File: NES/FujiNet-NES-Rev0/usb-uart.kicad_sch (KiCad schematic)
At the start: 13 parts, among them J3 USB-C, U10 CP2102N-A02-GQFN28, U11 UMH3N

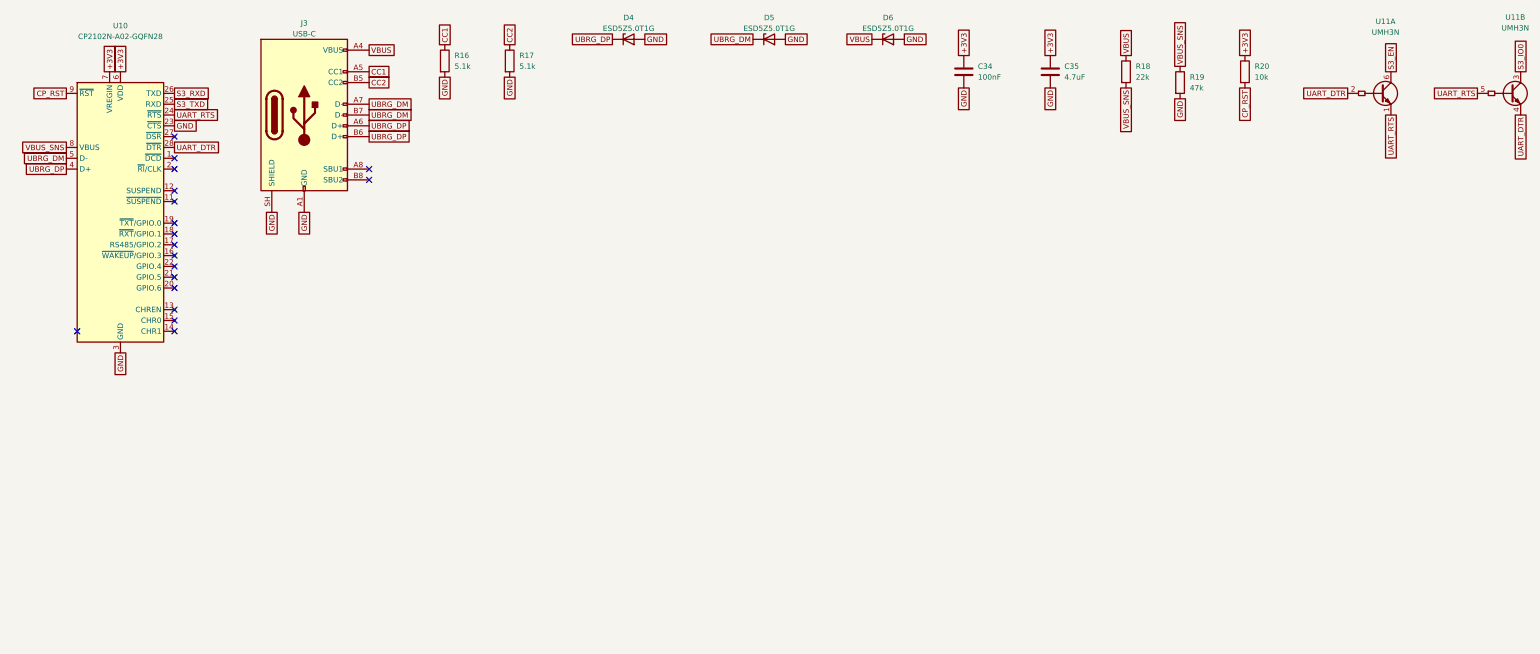
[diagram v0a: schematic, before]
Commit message: Nes rev0 (#48)
* NES: add the FujiNet-NES-Rev0 schematic

RP2354B on the 5 V cart bus with two AS6C4008-55 SRAMs (PRG, CHR) whose
bank lines come from the RP's PIO, 74HCT595/253/14/00/32 glue, and the
Astrocade Rev0 ESP32-S3, USB-UART and power sheets carried over.
Generated from tools/design.py the same way as Astrocade/rev0; ERC
reports no violations and tools/check_nets.py checks every GPIO, SRAM
line and decode equation against fujinet-firmware's nes_cart.h and
fujiversal-nes.h.

Schematic only: no layout, no board built, nothing run on a console.
The edge pinout follows the nesdev Cartridge connector page (pin 37 is
SYSTEM CLK, 2.50 mm pitch).

Co-Authored-By: Claude Fable 5.1 <noreply@anthropic.com>

* NES Rev0: audit the schematic with kicad-happy and redo it

Datasheet-backed review of the first Rev0 schematic (kicad-happy analyzer,
ngspice, 28 deep-review findings all evidence-gated, 453 netlist checks
against fujinet-firmware nes-bringup) and the fixes it called for:

- edge footprint was mirrored (pin 1 west); nesdev and two measured
  NES-EWROM-01 references put pin 1 east on the label side. Fingers are now
  2.0 x 12 mm (ends 3.0 at +/-44.25), 2.50 pitch, copper 1.0-13.0 mm in,
  Nintendo's front/back mask depths
- RP2350 pads are 5 V-tolerant only while IOVDD is powered: the IOVDD group
  moves to an AP2112K (20 us) rail +3V3_RP; VREG_VIN stays on the buck
- 74HCT595 /OE = NAND(PWR_OK, POR) with 100k pull-downs on every bit, so
  the register cannot enable the SRAMs before the RP loads it or while
  the console is off
- PRG /WE = NAND4(M2, ROMSEL, !R/W, PRG_WE_EN) on a CD74HCT20, one gate
  after M2 (was three after the console's /ROMSEL decoder vs ~30 ns hold)
- CIRAM /CE through the 74HCT253's second half, tri-stated by PWR_OK_N
- console 5 V through an AO3401A P-FET (gate = VBUS) instead of a Schottky
- console-sense divider 22k/100k (TI 74HCT14 VT+ reaches 0.70 x VCC)
- WS2812B-2020 on +5V (datasheet VDD 3.7-5.3 V, VIH 2.7 V)
- VBUS decoupling at t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
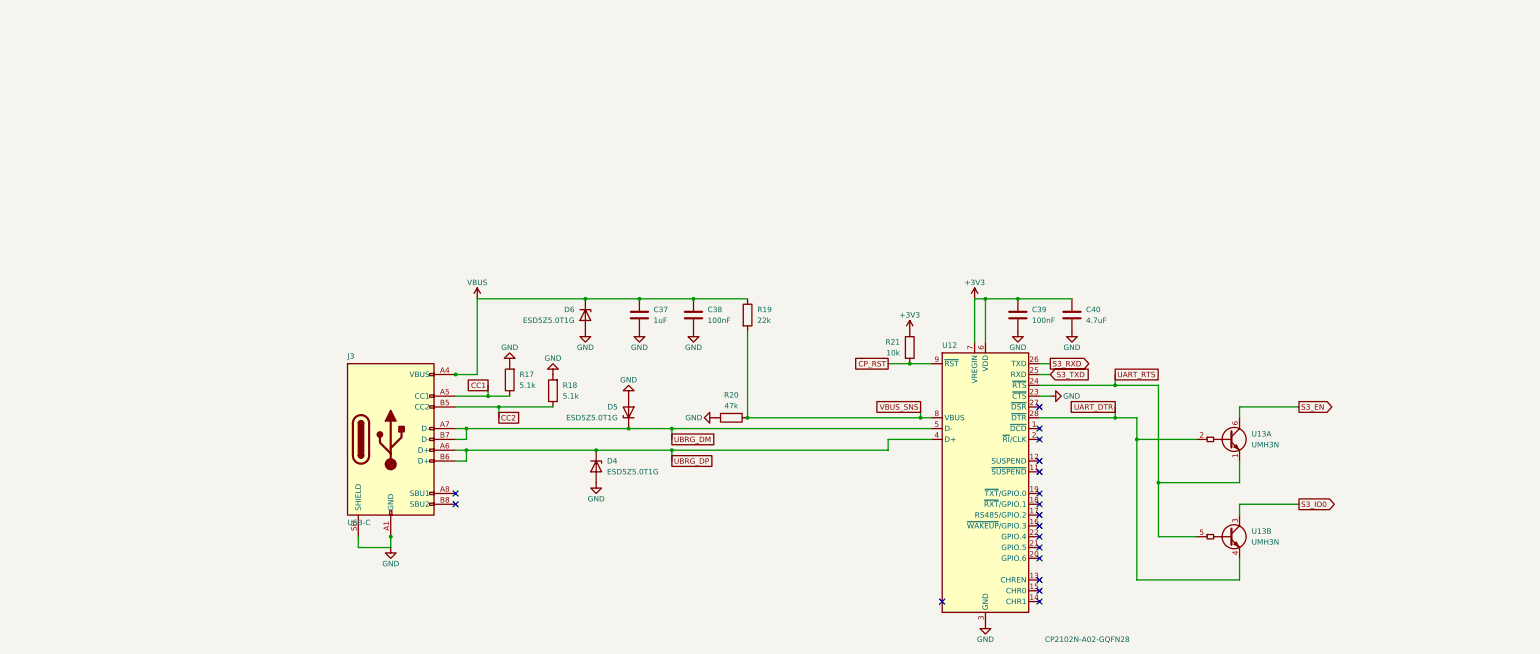
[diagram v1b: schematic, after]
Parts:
- removed C34: 100nF, FujiNet-NES:C_0603_1608Metric, symbol Device:C
- removed C35: 4.7uF, FujiNet-NES:C_0603_1608Metric, symbol Device:C
- removed R16: 5.1k, FujiNet-NES:R_0603_1608Metric, symbol Device:R
- removed U10: CP2102N-A02-GQFN28, FujiNet-NES:QFN-28-1EP_5x5mm_P0.5mm_EP3.35x3.35mm, symbol Interface_USB:CP2102N-Axx-xQFN28
- removed U11: UMH3N, FujiNet-NES:SOT-363_SC-70-6, symbol Transistor_BJT:UMH3N
- added C37: 1uF, FujiNet-NES:C_0603_1608Metric, symbol Device:C
- added C38, C39: 100nF, FujiNet-NES:C_0603_1608Metric, symbol Device:C
- added C40: 4.7uF, FujiNet-NES:C_0603_1608Metric, symbol Device:C
- added R21: 10k, FujiNet-NES:R_0603_1608Metric, symbol Device:R
- added U12: CP2102N-A02-GQFN28, FujiNet-NES:QFN-28-1EP_5x5mm_P0.5mm_EP3.35x3.35mm, symbol Interface_USB:CP2102N-Axx-xQFN28
- added U13: UMH3N, FujiNet-NES:SOT-363_SC-70-6, symbol Transistor_BJT:UMH3N
- R18: value 22k -> 5.1k; LCSC C31850 -> C23186; MPN 0603WAF2202T5E -> 0603WAF5101T5E
- R19: value 47k -> 22k; LCSC C25819 -> C31850; MPN 0603WAF4702T5E -> 0603WAF2202T5E
- R20: value 10k -> 47k; LCSC C25804 -> C25819; MPN 0603WAF1002T5E -> 0603WAF4702T5E
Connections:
- net +3V3: now also C39.1, C40.1, R21.1, U12.6 (VDD), U12.7 (VREGIN); no longer R20.1
- net CC1: now also R17.1
- net CC2: now also R18.1; no longer R17.1
- net CP_RST: now also R21.2, U12.9 (~{RST}); no longer R20.2
- net GND: now also R18.2, R20.2, C37.2, C38.2, C39.2, C40.2, U12.23 (~{CTS}), U12.29 (GND), U12.3 (GND); no longer R19.2
- net S3_EN: now also U13.6 (C1)
- net S3_IO0: now also U13.3 (C2)
- net S3_RXD: now also U12.26 (TXD)
- net S3_TXD: now also U12.25 (RXD)
- net UART_DTR: now also U12.28 (~{DTR}), U13.2 (B1), U13.4 (E2)
- net UART_RTS: now also U12.24 (~{RTS}), U13.1 (E1), U13.5 (B2)
- net UBRG_DM: now also U12.5 (D-)
- net UBRG_DP: now also U12.4 (D+)
- net VBUS: now also R19.1, C37.1, C38.1; no longer R18.1
- net VBUS_SNS: now also R19.2, R20.1, U12.8 (VBUS); no longer R18.2, R19.1
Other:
- title: FujiNet NES Rev0 - USB-C, CP2102N programming bridge -> FujiNet NES Rev0 - USB-C, CP2102N bridge
- moved on the sheet: D4, D5, D6, J3, R17, R18, R19, R20
